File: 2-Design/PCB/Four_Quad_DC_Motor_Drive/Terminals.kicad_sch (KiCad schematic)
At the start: 0 parts

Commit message: Added some more schematic symbols and three phase rectifier schematics
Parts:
- added J? (x7): 4mm_banana, symbol ee463_symbol_library:4mm_banana
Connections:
- new net Chopper1: J?.1
- new net Chopper2: J?.1
- new net MOTOR+: J?.1
- new net MOTOR-: J?.1
- new net PH_A: J?.1
- new net PH_B: J?.1
- new net PH_C: J?.1
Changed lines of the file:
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@@
 (kicad_sch (version 20211123) (generator eeschema)
   (paper "A4")
+  (title_block
+    (date "2022-12-20")
+  )
+  (wire (pts (xy 78.74 113.03) (xy 87.63 113.03))
+    (stroke (width 0) (type default) (color 0 0 0 0))
+  )
+  (wire (pts (xy 78.74 54.61) (xy 87.63 54.61))
+    (stroke (width 0) (type default) (color 0 0 0 0))
+  )
+  (wire (pts (xy 78.74 67.31) (xy 87.63 67.31))
+    (stroke (width 0) (type default) (color 0 0 0 0))
+  )
+  (wire (pts (xy 78.74 97.79) (xy 87.63 97.79))
+    (stroke (width 0) (type default) (color 0 0 0 0))
+  )
+  (wire (pts (xy 132.08 54.61) (xy 140.97 54.61))
+    (stroke (width 0) (type default) (color 0 0 0 0))
+  )
+  (wire (pts (xy 78.74 82.55) (xy 87.63 82.55))
+    (stroke (width 0) (type default) (color 0 0 0 0))
+  )
+  (wire (pts (xy 132.08 67.31) (xy 140.97 67.31))
+    (stroke (width 0) (type default) (color 0 0 0 0))
+  )
+  (global_label "MOTOR-" (shape input) (at 140.97 67.31 0) (fields_autoplaced)
+    (effects (font (size 1.27 1.27)) (justify left))
+    (property "Intersheet References" "${INTERSHEET_REFS}" (id 0) (at 151.3055 67.2306 0)
+      (effects (font (size 1.27 1.27)) (justify left) hide)
+    )
+  )
+  (global_label "MOTOR+" (shape input) (at 140.97 54.61 0) (fields_autoplaced)
+    (effects (font (size 1.27 1.27)) (justify left))
+    (property "Intersheet References" "${INTERSHEET_REFS}" (id 0) (at 151.3055 54.5306 0)
+      (effects (font (size 1.27 1.27)) (justify left) hide)
+    )
+  )
+  (global_label "Chopper2" (shape input) (at 87.63 113.03 0) (fields_autoplaced)
+    (effects (font (size 1.27 1.27)) (justify left))
+    (property "Intersheet References" "${INTERSHEET_REFS}" (id 0) (at 98.9936 112.9506 0)
+      (effects (font (size 1.27 1.27)) (justify left) hide)
+    )
+  )
+  (global_label "Chopper1" (shape input) (at 87.63 97.79 0) (fields_autoplaced)
+    (effects (font (size 1.27 1.27)) (justify left))
+    (property "Intersheet References" "${INTERSHEET_REFS}" (id 0) (at 98.9936 97.7106 0)
+      (effects (font (size 1.27 1.27)) (justify left) hide)
+    )
+  )
+  (global_label "PH_B" (shape input) (at 87.63 67.31 0) (fields_autoplaced)
+    (effects (font (size 1.27 1.27)) (justify left))
+    (property "Intersheet References" "${INTERSHEET_REFS}" (id 0) (at 94.8812 67.2306 0)
+      (effects (font (size 1.27 1.27)) (justify left) hide)
+    )
+  )
+  (global_label "PH_A" (shape input) (at 87.63 54.61 0) (fields_autoplaced)
+    (effects (font (size 1.27 1.27)) (justify left))
+    (property "Intersheet References" "${INTERSHEET_REFS}" (id 0) (at 94.6998 54.5306 0)
+      (effects (font (size 1.27 1.27)) (justify left) hide)
+    )
+  )
+  (global_label "PH_C" (shape input) (at 87.63 82.55 0) (fields_autoplaced)
+    (effects (font (size 1.27 1.27)) (justify left))
+    (property "Intersheet References" "${INTERSHEET_REFS}" (id 0) (at 94.8812 82.4706 0)
+      (effects (font (size 1.27 1.27)) (justify left) hide)
+    )
+  )
+  (symbol (lib_id "ee463_symbol_library:4mm_banana") (at 73.66 82.55 180) (unit 1)
+    (in_bom yes) (on_board yes) (fields_autoplaced)
+    (property "Reference" "J?" (id 0) (at 73.66 74.93 0))
+    (property "Value" "4mm_banana" (id 1) (at 73.66 77.47 0))
+    (property "Footprint" "" (id 2) (at 73.66 82.55 0)
+      (effects (font (size 1.27 1.27)) hide)
+    )
+    (property "Datasheet" "" (id 3) (at 73.66 82.55 0)
+      (effects (font (size 1.27 1.27)) hide)
+    )
+    (pin "1")
+  )
+  (symbol (lib_id "ee463_symbol_library:4mm_banana") (at 73.66 67.31 180) (unit 1)
+    (in_bom yes) (on_board yes) (fields_autoplaced)
+    (property "Reference" "J?" (id 0) (at 73.66 59.69 0))
+    (property "Value" "4mm_banana" (id 1) (at 73.66 62.23 0))
+    (property "Footprint" "" (id 2) (at 73.66 67.31 0)
+      (effects (font (size 1.27 1.27)) hide)
+    )
+    (property "Datasheet" "" (id 3) (at 73.66 67.31 0)
+      (effects (font (size 1.27 1.27)) hide)
+    )
+    (pin "1")
+  )
+  (symbol (lib_id "ee463_symbol_library:4mm_banana") (at 73.66 54.61 180) (unit 1)
+    (in_bom yes) (on_board yes) (fields_autoplaced)
+    (property "Reference" "J?" (id 0) (at 73.66 46.99 0))
+    (property "Value" "4mm_banana" (id 1) (at 73.66 49.53 0))
+    (property "Footprint" "" (id 2) (at 73.66 54.61 0)
+      (effects (font (size 1.27 1.27)) hide)
+    )
+    (property "Datasheet" "" (id 3) (at 73.66 54.61 0)
+      (effects (font (size 1.27 1.27)) hide)
+    )
+    (pin "1")
+  )
+  (symbol (lib_id "ee463_symbol_library:4mm_banana") (at 73.66 97.79 180) (unit 1)
+    (in_bom yes) (on_board yes) (fields_autoplaced)
+    (property "Reference" "J?" (id 0) (at 73.66 90.17 0))
+    (property "Value" "4mm_banana" (id 1) (at 73.66 92.71 0))
+    (property "Footprint" "" (id 2) (at 73.66 97.79 0)
+      (effects (font (size 1.27 1.27)) hide)
+    )
+    (property "Datasheet" "" (id 3) (at 73.66 97.79 0)
+      (effects (font (size 1.27 1.27)) hide)
+    )
+    (pin "1")
+  )
+  (symbol (lib_id "ee463_symbol_library:4mm_banana") (at 73.66 113.03 180) (unit 1)
+    (in_bom yes) (on_board yes) (fields_autoplaced)
+    (property "Reference" "J?" (id 0) (at 73.66 105.41 0))
+    (property "Value" "4mm_banana" (id 1) (at 73.66 107.95 0))
+    (property "Footprint" "" (id 2) (at 73.66 113.03 0)
+      (effects (font (size 1.27 1.27)) hide)
+    )
+    (property "Datasheet" "" (id 3) (at 73.66 113.03 0)
+      (effects (font (size 1.27 1.27)) hide)
+    )
+    (pin "1")
+  )
+  (symbol (lib_id "ee463_symbol_library:4mm_banana") (at 127 67.31 180) (unit 1)
+    (in_bom yes) (on_board yes) (fields_autoplaced)
+    (property "Reference" "J?" (id 0) (at 127 59.69 0))
+    (property "Value" "4mm_banana" (id 1) (at 127 62.23 0))
+    (property "Footprint" "" (id 2) (at 127 67.31 0)
+      (effects (font (size 1.27 1.27)) hide)
+    )
+    (property "Datasheet" "" (id 3) (at 127 67.31 0)
+      (effects (font (size 1.27 1.27)) hide)
+    )
+    (pin "1")
+  )
+  (symbol (lib_id "ee463_symbol_library:4mm_banana") (at 127 54.61 180) (unit 1)
+    (in_bom yes) (on_board yes) (fields_autoplaced)
+    (property "Reference" "J?" (id 0) (at 127 46.99 0))
+    (property "Value" "4mm_banana" (id 1) (at 127 49.53 0))
+    (property "Footprint" "" (id 2) (at 127 54.61 0)
+      (effects (font (size 1.27 1.27)) hide)
+    )
+    (property "Datasheet" "" (id 3) (at 127 54.61 0)
+      (effects (font (size 1.27 1.27)) hide)
+    )
+    (pin "1")
+  )
 )

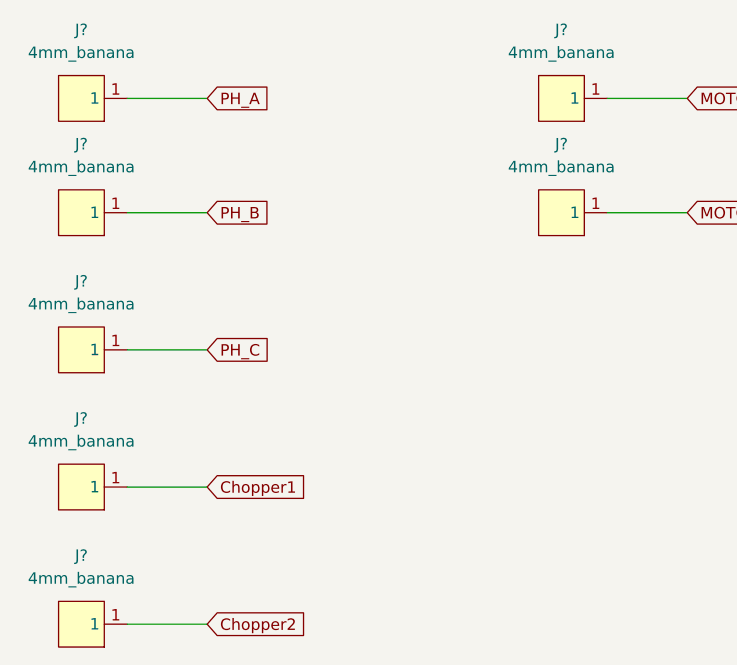
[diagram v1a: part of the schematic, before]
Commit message: Added the label and gate drive resistances
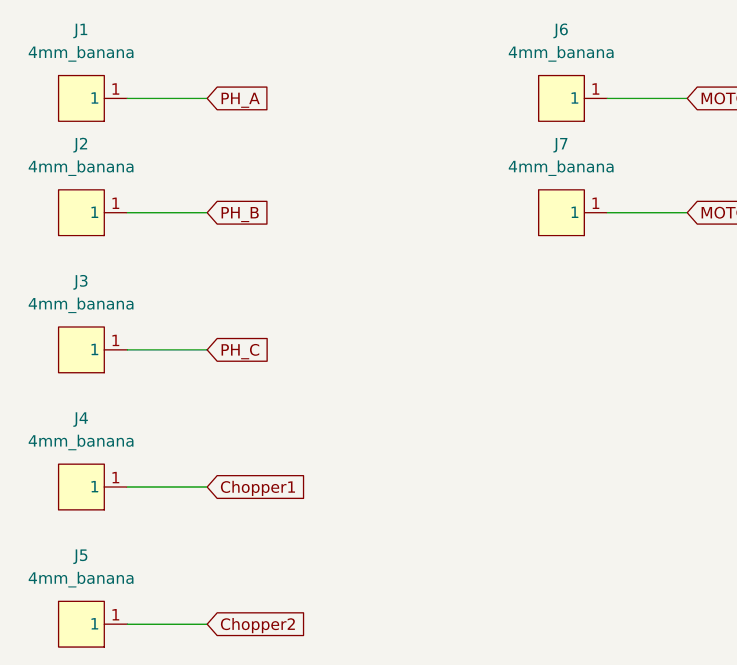
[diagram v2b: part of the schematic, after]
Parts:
- gave numbers to parts that had none: 7
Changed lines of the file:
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@@
   (symbol (lib_id "ee463_symbol_library:4mm_banana") (at 73.66 82.55 180) (unit 1)
     (in_bom yes) (on_board yes) (fields_autoplaced)
-    (property "Reference" "J?" (id 0) (at 73.66 74.93 0))
+    (property "Reference" "J3" (id 0) (at 73.66 74.93 0))
     (property "Value" "4mm_banana" (id 1) (at 73.66 77.47 0))
     (property "Footprint" "" (id 2) (at 73.66 82.55 0)
@@
   (symbol (lib_id "ee463_symbol_library:4mm_banana") (at 73.66 67.31 180) (unit 1)
     (in_bom yes) (on_board yes) (fields_autoplaced)
-    (property "Reference" "J?" (id 0) (at 73.66 59.69 0))
+    (property "Reference" "J2" (id 0) (at 73.66 59.69 0))
     (property "Value" "4mm_banana" (id 1) (at 73.66 62.23 0))
     (property "Footprint" "" (id 2) (at 73.66 67.31 0)
@@
   (symbol (lib_id "ee463_symbol_library:4mm_banana") (at 73.66 54.61 180) (unit 1)
     (in_bom yes) (on_board yes) (fields_autoplaced)
-    (property "Reference" "J?" (id 0) (at 73.66 46.99 0))
+    (property "Reference" "J1" (id 0) (at 73.66 46.99 0))
     (property "Value" "4mm_banana" (id 1) (at 73.66 49.53 0))
     (property "Footprint" "" (id 2) (at 73.66 54.61 0)
@@
   (symbol (lib_id "ee463_symbol_library:4mm_banana") (at 73.66 97.79 180) (unit 1)
     (in_bom yes) (on_board yes) (fields_autoplaced)
-    (property "Reference" "J?" (id 0) (at 73.66 90.17 0))
+    (property "Reference" "J4" (id 0) (at 73.66 90.17 0))
     (property "Value" "4mm_banana" (id 1) (at 73.66 92.71 0))
     (property "Footprint" "" (id 2) (at 73.66 97.79 0)
@@
   (symbol (lib_id "ee463_symbol_library:4mm_banana") (at 73.66 113.03 180) (unit 1)
     (in_bom yes) (on_board yes) (fields_autoplaced)
-    (property "Reference" "J?" (id 0) (at 73.66 105.41 0))
+    (property "Reference" "J5" (id 0) (at 73.66 105.41 0))
     (property "Value" "4mm_banana" (id 1) (at 73.66 107.95 0))
     (property "Footprint" "" (id 2) (at 73.66 113.03 0)
@@
   (symbol (lib_id "ee463_symbol_library:4mm_banana") (at 127 67.31 180) (unit 1)
     (in_bom yes) (on_board yes) (fields_autoplaced)
-    (property "Reference" "J?" (id 0) (at 127 59.69 0))
+    (property "Reference" "J7" (id 0) (at 127 59.69 0))
     (property "Value" "4mm_banana" (id 1) (at 127 62.23 0))
     (property "Footprint" "" (id 2) (at 127 67.31 0)
@@
   (symbol (lib_id "ee463_symbol_library:4mm_banana") (at 127 54.61 180) (unit 1)
     (in_bom yes) (on_board yes) (fields_autoplaced)
-    (property "Reference" "J?" (id 0) (at 127 46.99 0))
+    (property "Reference" "J6" (id 0) (at 127 46.99 0))
     (property "Value" "4mm_banana" (id 1) (at 127 49.53 0))
     (property "Footprint" "" (id 2) (at 127 54.61 0)

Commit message: Gate driver changed, plus other rearrangements on the schematics
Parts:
- J1: footprint (none) -> ee463_footprint_lib:4mm_banana
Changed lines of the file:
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@@
     (property "Reference" "J1" (id 0) (at 73.66 46.99 0))
     (property "Value" "4mm_banana" (id 1) (at 73.66 49.53 0))
-    (property "Footprint" "" (id 2) (at 73.66 54.61 0)
+    (property "Footprint" "ee463_footprint_lib:4mm_banana" (id 2) (at 73.66 54.61 0)
       (effects (font (size 1.27 1.27)) hide)
     )

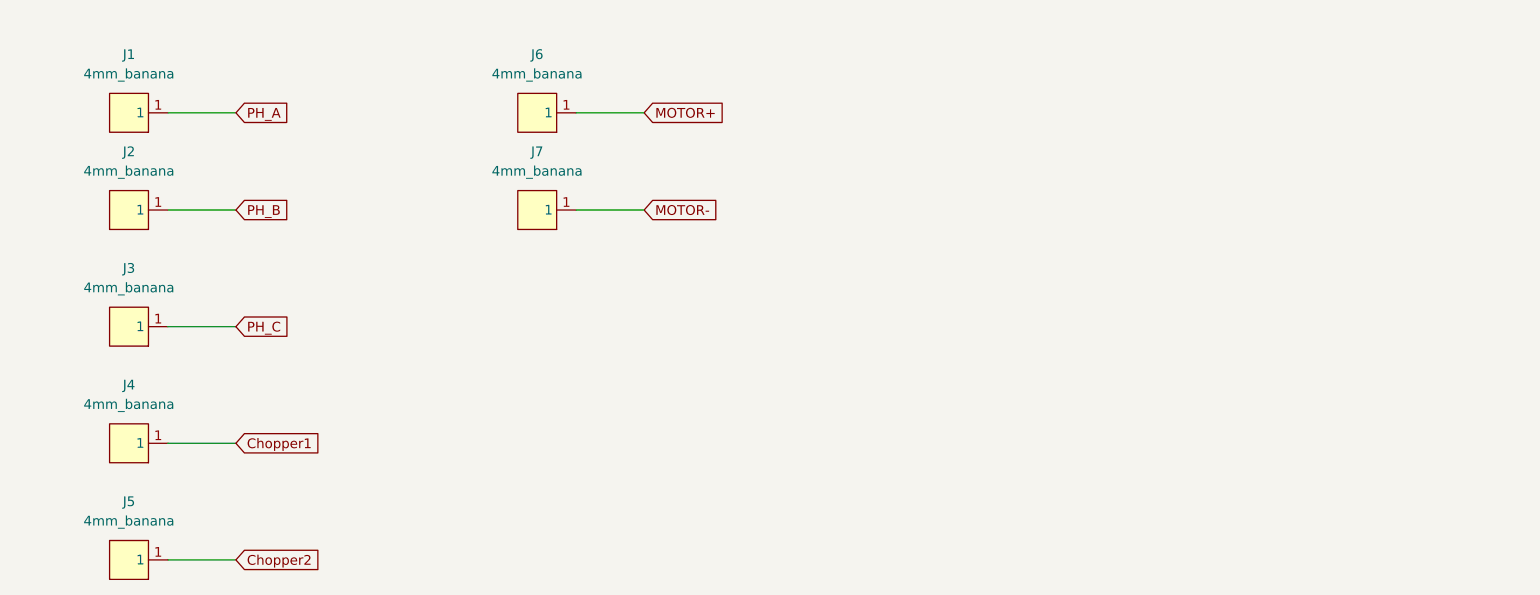
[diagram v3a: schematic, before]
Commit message: Gate drivers finished, controller pins to be arranged
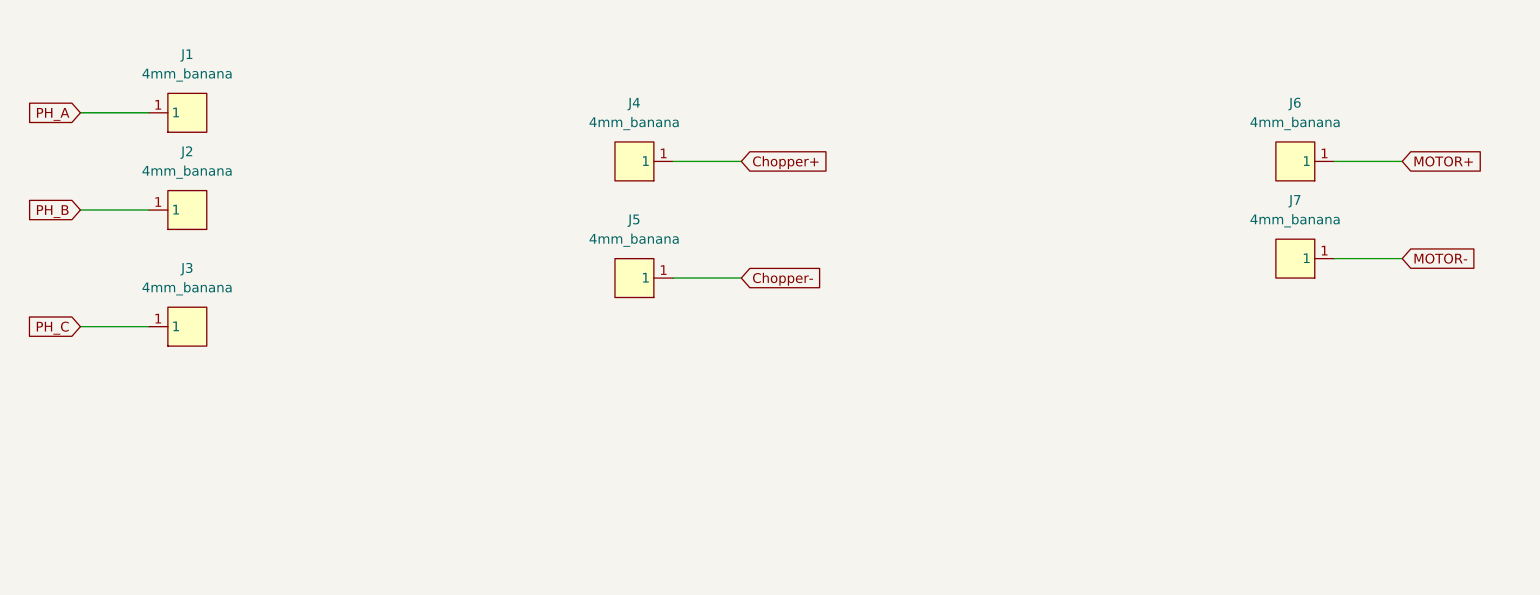
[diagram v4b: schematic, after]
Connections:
- net Chopper1 renamed Chopper+
- net Chopper2 renamed Chopper-
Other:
- moved on the sheet: J1, J2, J3, J4, J5, J6, J7

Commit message: Random Checkpoint
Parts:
- added C?: 1nF, Capacitor_SMD:C_1206_3216Metric_Pad1.33x1.80mm_HandSolder, symbol Device:C_Small
- added C?: 0.1uF, Capacitor_SMD:C_1206_3216Metric_Pad1.33x1.80mm_HandSolder, symbol Device:C_Small
- added R?: ???, symbol Device:R_Small_US
- added U?: ACS712xLCTR-30A, Package_SO:SOIC-8_3.9x4.9mm_P1.27mm, symbol Sensor_Current:ACS712xLCTR-30A
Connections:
- net MOTOR+: now also U?.1 (IP+), U?.2 (IP+); no longer J6.1
- new net: C?.2, U?.6 (FILTER)
- new net: R?.1, U?.7 (VIOUT)
- new net: J6.1, U?.3 (IP-), U?.4 (IP-)
- new net +5V: C?.1, U?.8 (VCC)
- new net GND: C?.1, C?.2, U?.5 (GND)
- new net I_sense: R?.2
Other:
- moved on the sheet: J6, J7
